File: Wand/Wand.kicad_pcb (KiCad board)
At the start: 4 copper layers, 50 x 7 mm, 20 parts, among them P1 ISP, P2 KLB4, P3 BASE, U1 ATMEGA328-MMH, U2 MAX31855KASA+, U3 MPU-6050

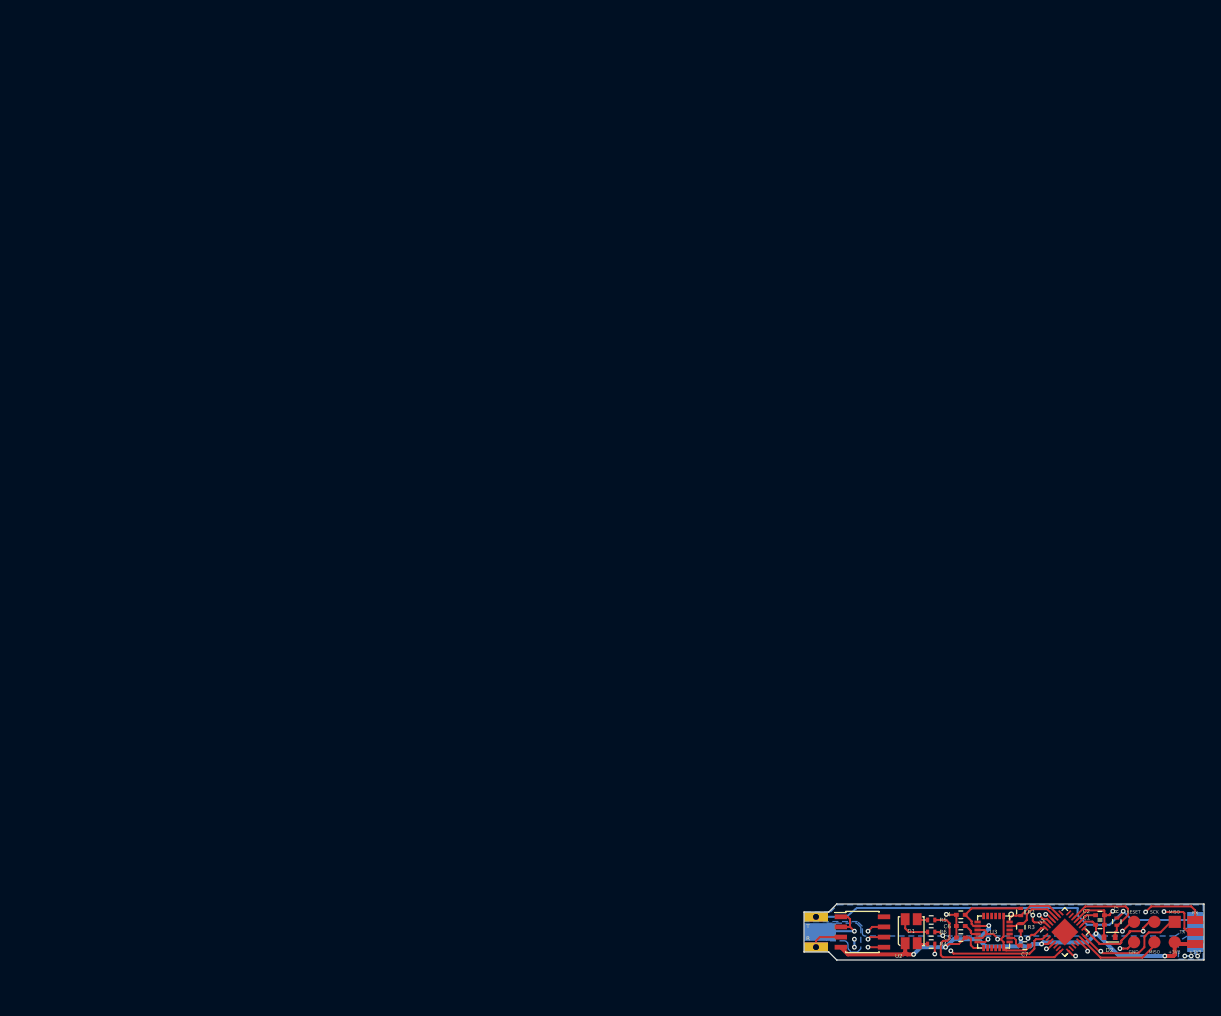
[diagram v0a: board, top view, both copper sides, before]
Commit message: Initial re-layout of the Hotstick Wand.
- Fixed tip connector
- Fixed the vias under the MPU-6050
- Changed to use an op-amp to read the tip temp
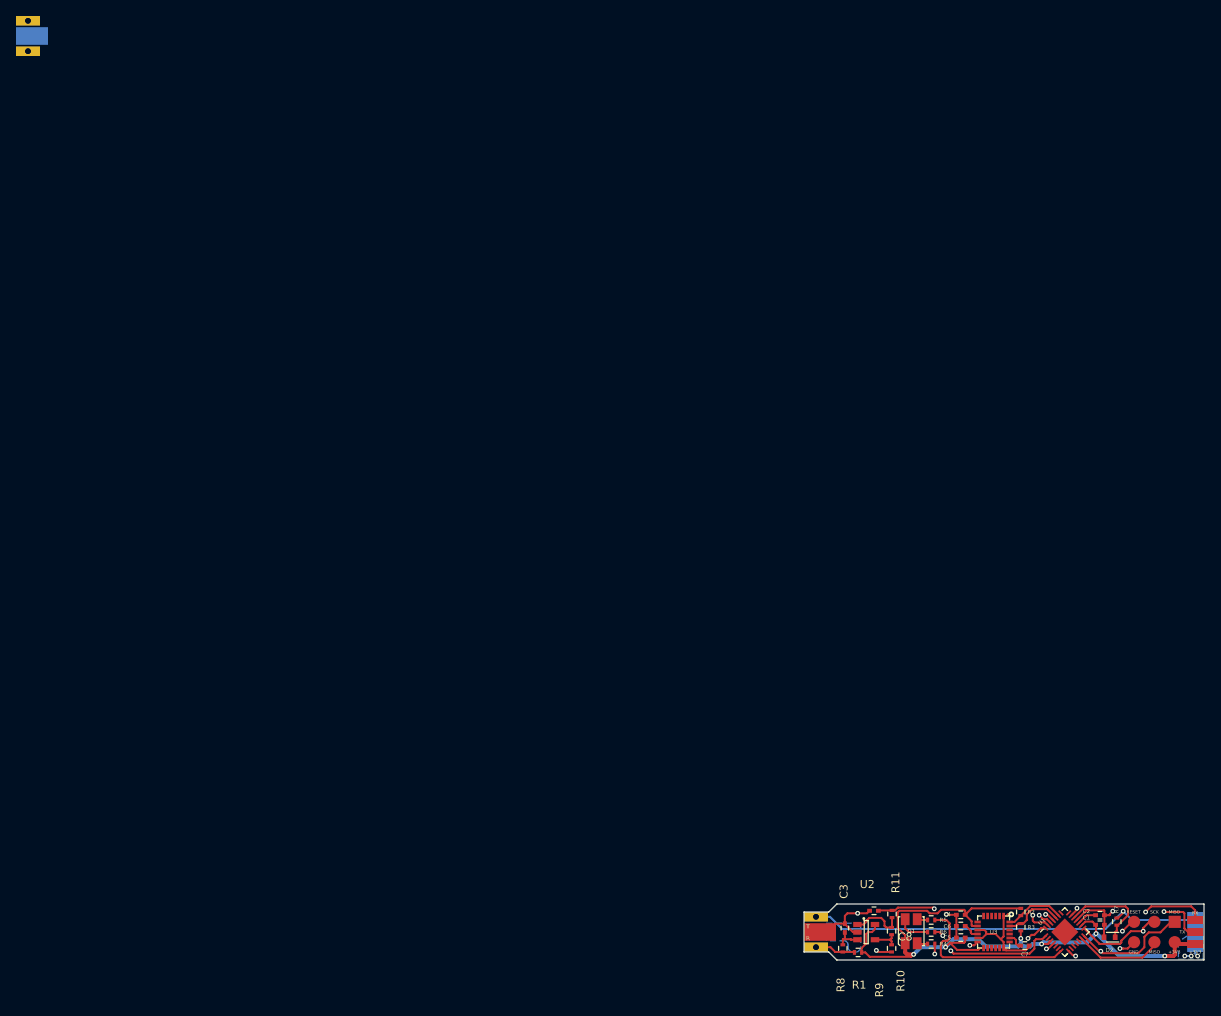
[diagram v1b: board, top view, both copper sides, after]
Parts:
- added C3: 100n, Capacitors_SMD:C_0402, F.Cu at (102.1, 111.5)
- added C8: 100n, Capacitors_SMD:C_0402, F.Cu at (105.7, 109.3)
- added P2: KLB4, Jack_3.5mm_KLB, F.Cu at (0.00, 0.00)
- added R1: 1M, Resistors_SMD:R_0402, F.Cu at (103.8, 114.6)
- added R10: 56K, Resistors_SMD:R_0402, F.Cu at (108.0, 111.9)
- added R11: 1K, Resistors_SMD:R_0402, F.Cu at (108.0, 109.8)
- added R8: 1K, Resistors_SMD:R_0402, F.Cu at (101.9, 114.0)
- added R9: 100R, Resistors_SMD:R_0402, F.Cu at (108.0, 114.0)
- D2: value 3V3 -> MM5Z3V3T1G
- U2: value MAX31855KASA+ -> OPA336; footprint Housings_SOIC:SOIC-8_3.9x4.9mm_Pitch1.27mm -> TO_SOT_Packages_SMD:SOT-23-5
- moved U2 0.48 mm to (104.8, 112.0)
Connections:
- U1 pad 12: /TIP_TEMP_SELECT -> (no net)
- U1 pad 20: (no net) -> /TEMP
- U2 pad 1: GND -> Net-(R10-Pad1)
- U2 pad 3: /SENS -> Net-(C3-Pad1)
- U2 pad 4: +3V3 -> Net-(R10-Pad2)
- U2 pad 5: /SCK -> +3V3
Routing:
- net /SCK: track 52.7 -> 11.2 mm, vias 2 -> 1
- net /TIP_TEMP_SELECT: track 34.4 -> 0.00 mm, vias 2 -> 0
- net /MISO: track 49.1 -> 14.7 mm, vias 2 -> 1
- net /TEMP: track 0.00 -> 26.6 mm, vias 0 -> 2
- net +3V3: track 78.8 -> 92.9 mm, vias 7 -> 6
- net GND: track 95.1 -> 103.9 mm, vias 11 -> 10
- net Net-(R10-Pad1): track 0.00 -> 6.79 mm
- net Net-(C3-Pad1): track 0.00 -> 3.39 mm
- net Net-(R10-Pad2): track 0.00 -> 3.31 mm
- net /MPU_INT: track 10.9 -> 11.9 mm
- net /SENS: track 4.09 -> 5.08 mm
- net /HEAT: track 51.6 -> 50.7 mm
- removed copper zone on B.Cu, net /HEAT

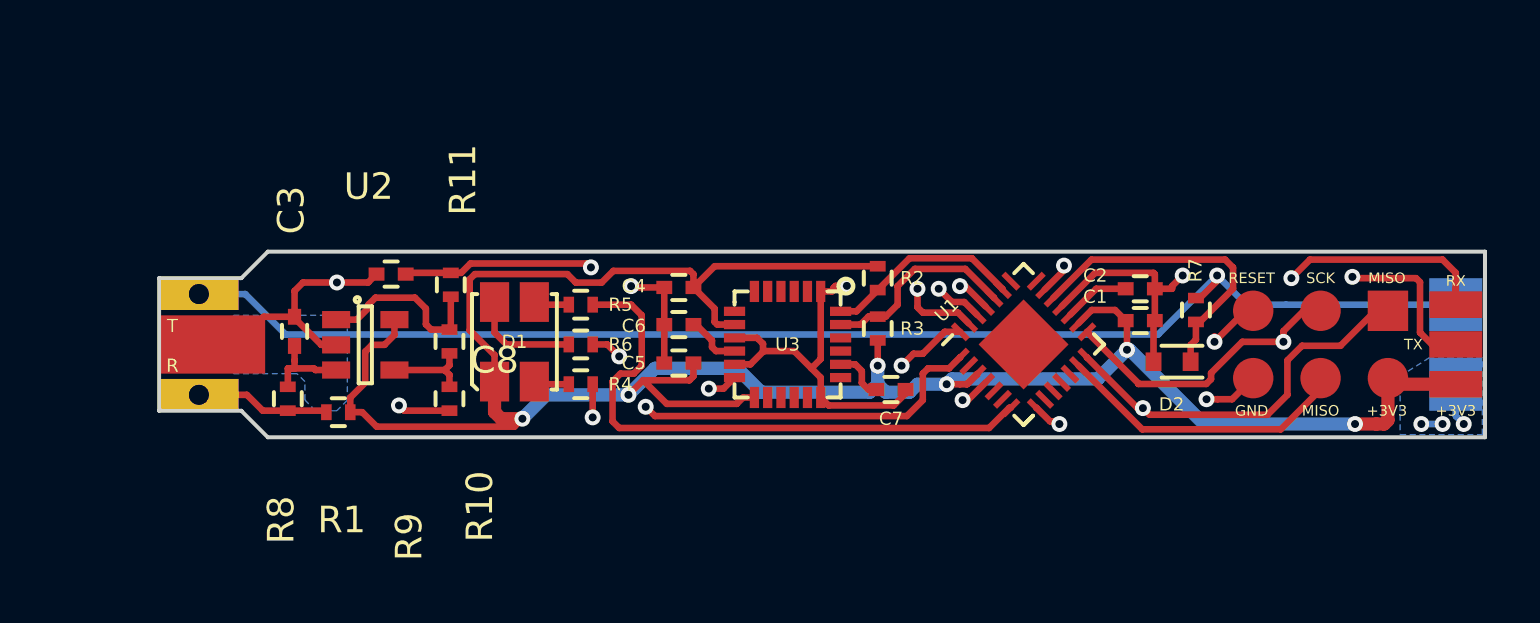
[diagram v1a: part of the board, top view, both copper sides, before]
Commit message: Added copper fills
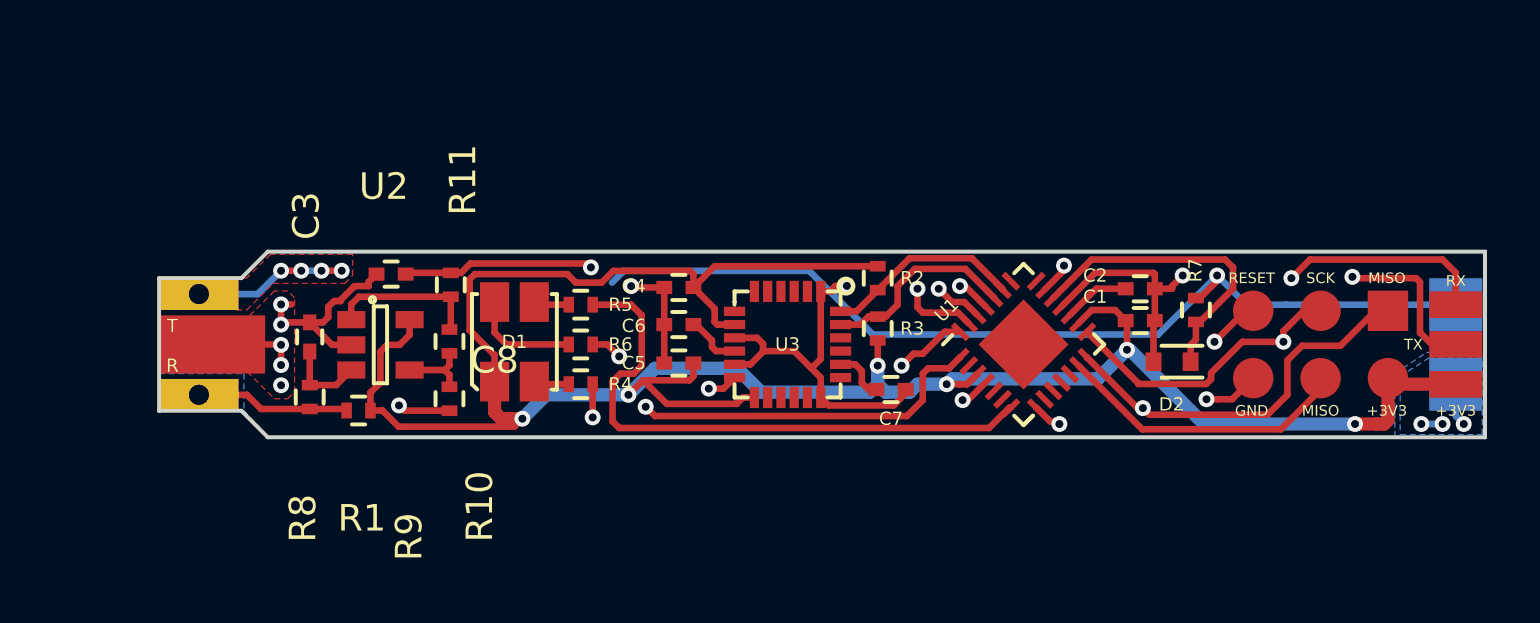
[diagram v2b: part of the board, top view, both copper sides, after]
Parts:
- moved R8 0.83 mm to (102.7, 114.0)
- moved R1 0.76 mm to (104.5, 114.5)
- moved C3 0.61 mm to (102.7, 111.7)
- moved U2 0.57 mm to (105.3, 112.0)
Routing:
- net /HEAT: track 50.7 -> 41.4 mm, vias 1 -> 5
- net GND: track 103.9 -> 107.0 mm, vias 10 -> 14
- net Net-(R10-Pad1): track 6.79 -> 5.71 mm
- net +3V3: track 92.9 -> 92.0 mm
- net /SENS: track 5.08 -> 5.82 mm
- net Net-(R10-Pad2): track 3.31 -> 2.73 mm
- added copper zone on B.Cu, net /HEAT
- added copper zone on F.Cu, net /HEAT
- added copper zone on F.Cu, net GND

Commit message: Tidy up of the silk screen
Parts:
- removed the P2 at (0.00, 0.00)
- added G***: LOGO, Wand:RLAB_LOGO, B.Cu at (108.7, 112.0)
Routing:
- net /RX: track 24.3 -> 23.7 mm
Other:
- board text added: "rev 2 - 18/09/2016"
- board text removed: "rev 1 - 26/01/2016"
